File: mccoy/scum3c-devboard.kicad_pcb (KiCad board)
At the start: 2 copper layers, 42.5 x 34.3 mm, 51 parts, among them J1 Conn_02x08_Odd_Even, J10 through_hole, J11 through_hole, J12 through_hole, J13 through_hole, J14 through_hole, J15 through_hole, J16 through_hole, J17 through_hole, J18 through_hole, J19 through_hole, J2 Conn_02x10_Odd_Even, J20 through_hole, J21 through_hole, J3 Conn_02x05_Odd_Even, J4 Conn_01x01_Male, J5 through_hole, J6 through_hole, J7 through_hole, J8 through_hole, J9 through_hole, U1 scum3, U2 TPS60500DGS, U9AB1 ICM-20948

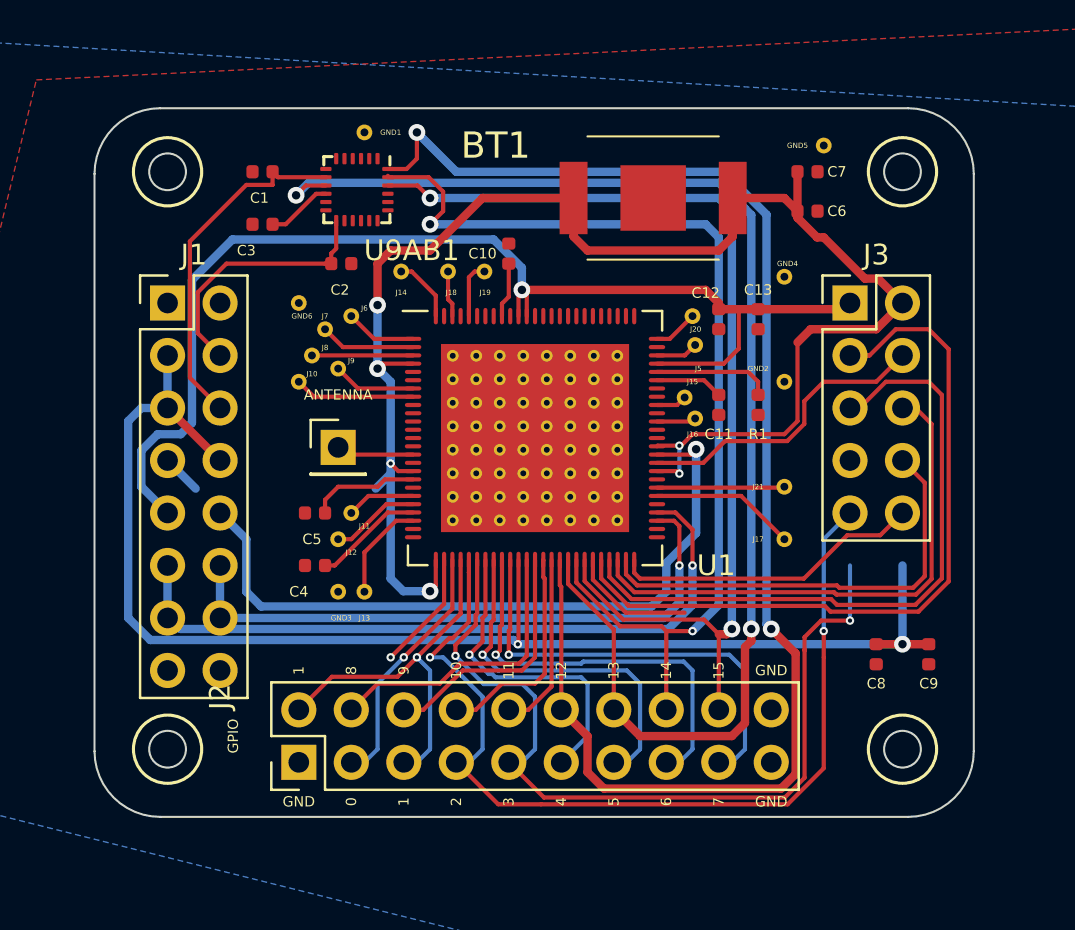
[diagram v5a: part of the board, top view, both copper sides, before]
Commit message: cleared all tracks
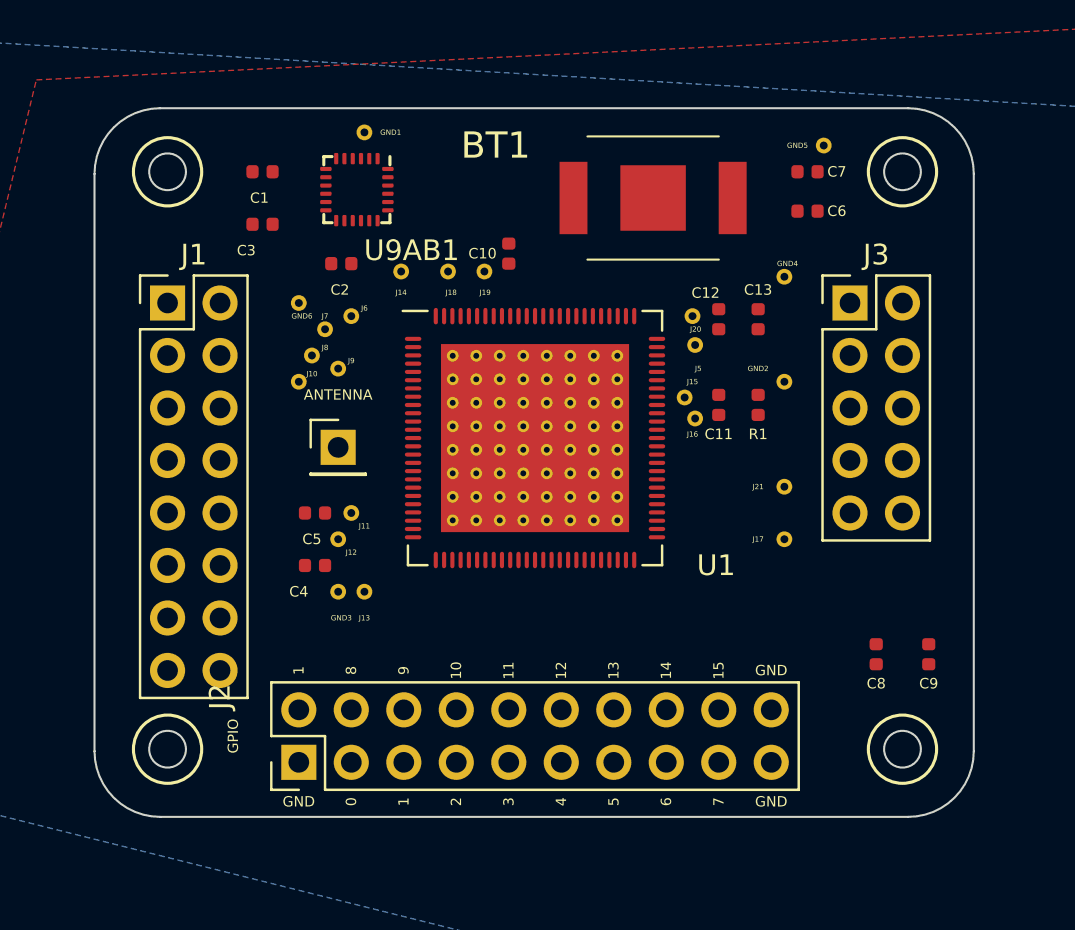
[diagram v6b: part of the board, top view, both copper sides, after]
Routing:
- net +VBAT: track 80.0 -> 0.00 mm, vias 6 -> 0
- net /GPIO12: track 70.6 -> 0.00 mm, vias 2 -> 0
- net +VDDIO: track 66.3 -> 0.00 mm, vias 2 -> 0
- net /GPIO13: track 64.6 -> 0.00 mm, vias 2 -> 0
- net +VDDD: track 57.3 -> 0.00 mm, vias 1 -> 0
- net /GPIO15: track 50.4 -> 0.00 mm, vias 2 -> 0
- net /GPIO14: track 50.2 -> 0.00 mm, vias 2 -> 0
- net /GPIO2: track 45.2 -> 0.00 mm, vias 2 -> 0
- net /GPIO3: track 41.3 -> 0.00 mm, vias 2 -> 0
- net /RsTx: track 36.0 -> 0.00 mm
- net /BOOT_SOURCE_SEL: track 35.0 -> 0.00 mm, vias 1 -> 0
- net /SENSOR_EXT_IN: track 34.3 -> 0.00 mm, vias 1 -> 0
- net /RsRx: track 32.1 -> 0.00 mm
- net /SENSOR_LDO_OUTPUT: track 29.6 -> 0.00 mm, vias 1 -> 0
- net /3WB_CLK: track 25.9 -> 0.00 mm
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
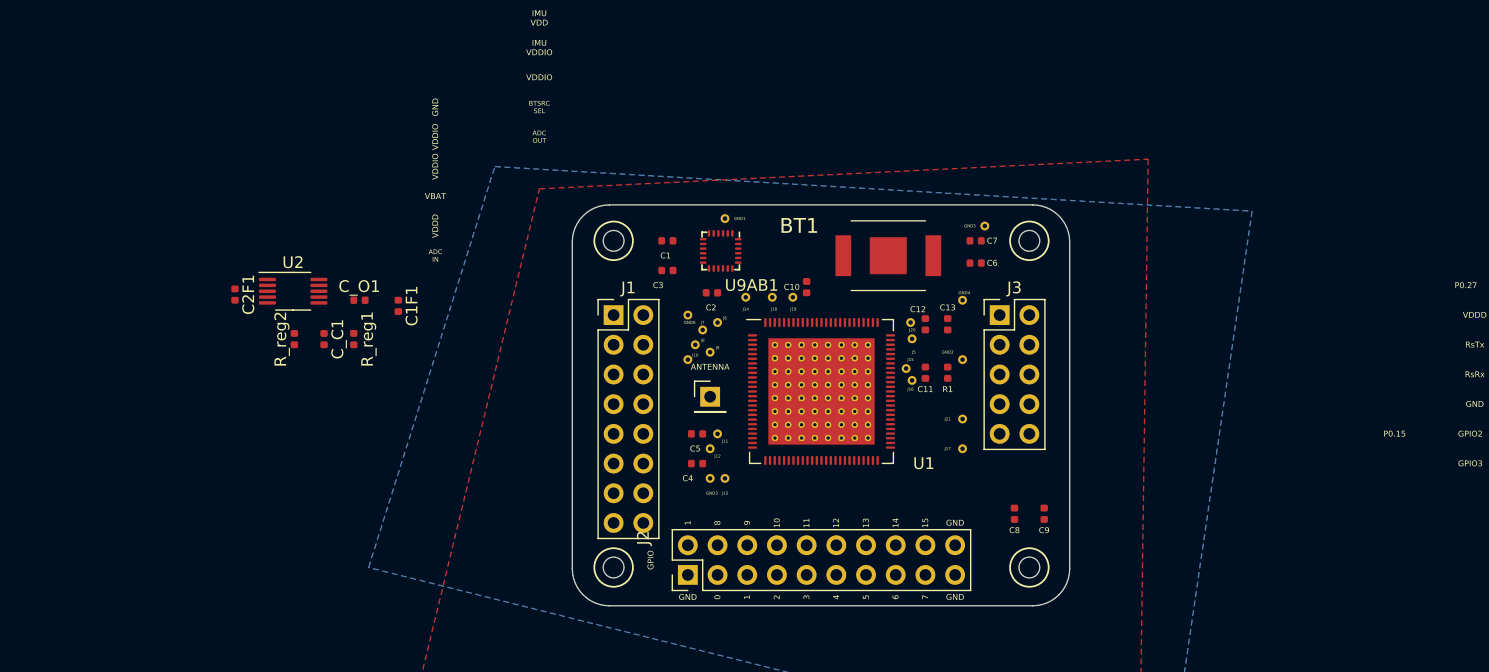
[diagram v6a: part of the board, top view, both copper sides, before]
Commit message: moved some footprints
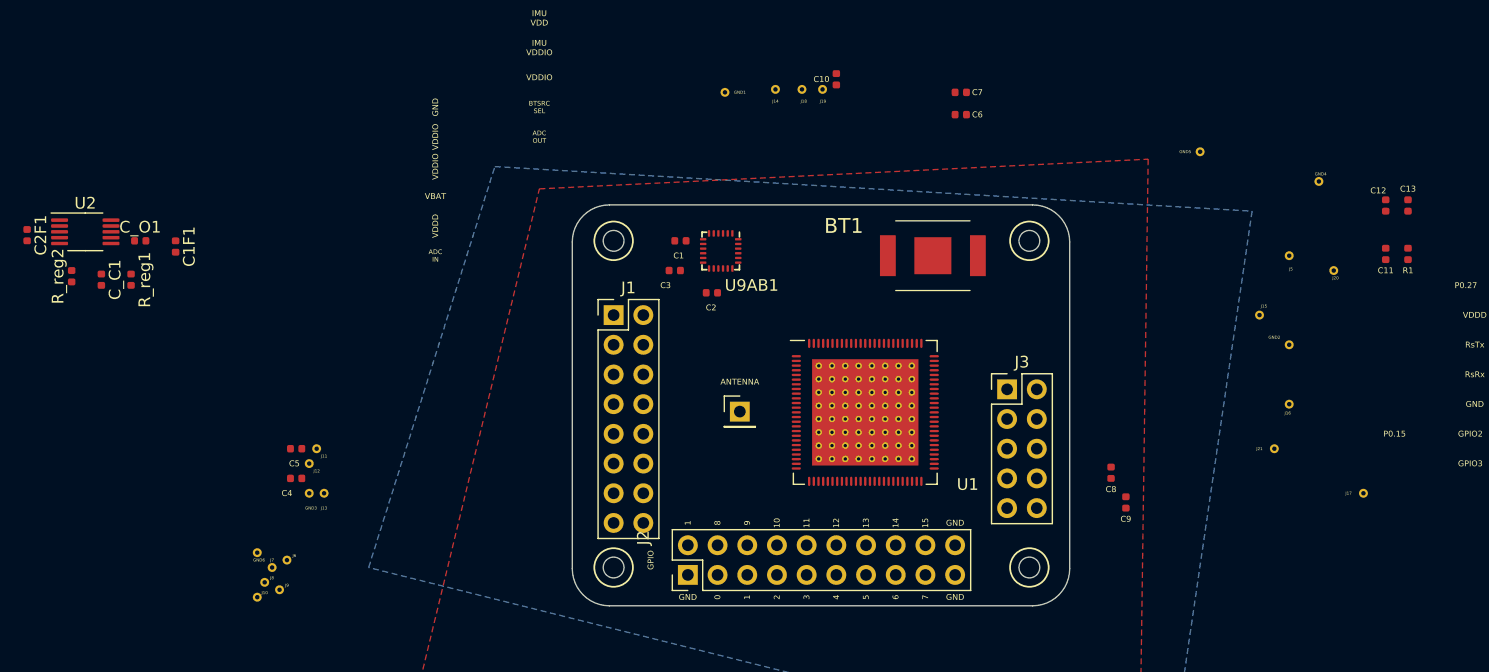
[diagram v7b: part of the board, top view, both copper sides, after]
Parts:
- moved GND6 42.1 mm to (78.1, 104.1)
- moved J10 42.1 mm to (78.1, 108.0)
- moved J6 42.1 mm to (80.6, 104.8)
- moved J8 42.1 mm to (78.7, 106.7)
- moved J7 42.1 mm to (79.4, 105.4)
- moved J9 42.1 mm to (80.0, 107.3)
- moved C11 40.7 mm to (174.6, 78.6)
- moved C12 40.7 mm to (174.6, 74.4)
- moved C13 40.7 mm to (176.5, 74.4)
- moved R1 40.7 mm to (176.5, 78.6)
- moved J20 36.5 mm to (170.2, 80.0)
- moved J17 34.5 mm to (172.7, 99.1)
- moved GND3 34.3 mm to (82.5, 99.1)
- moved J12 34.3 mm to (82.5, 96.5)
- moved J13 34.3 mm to (83.8, 99.1)
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
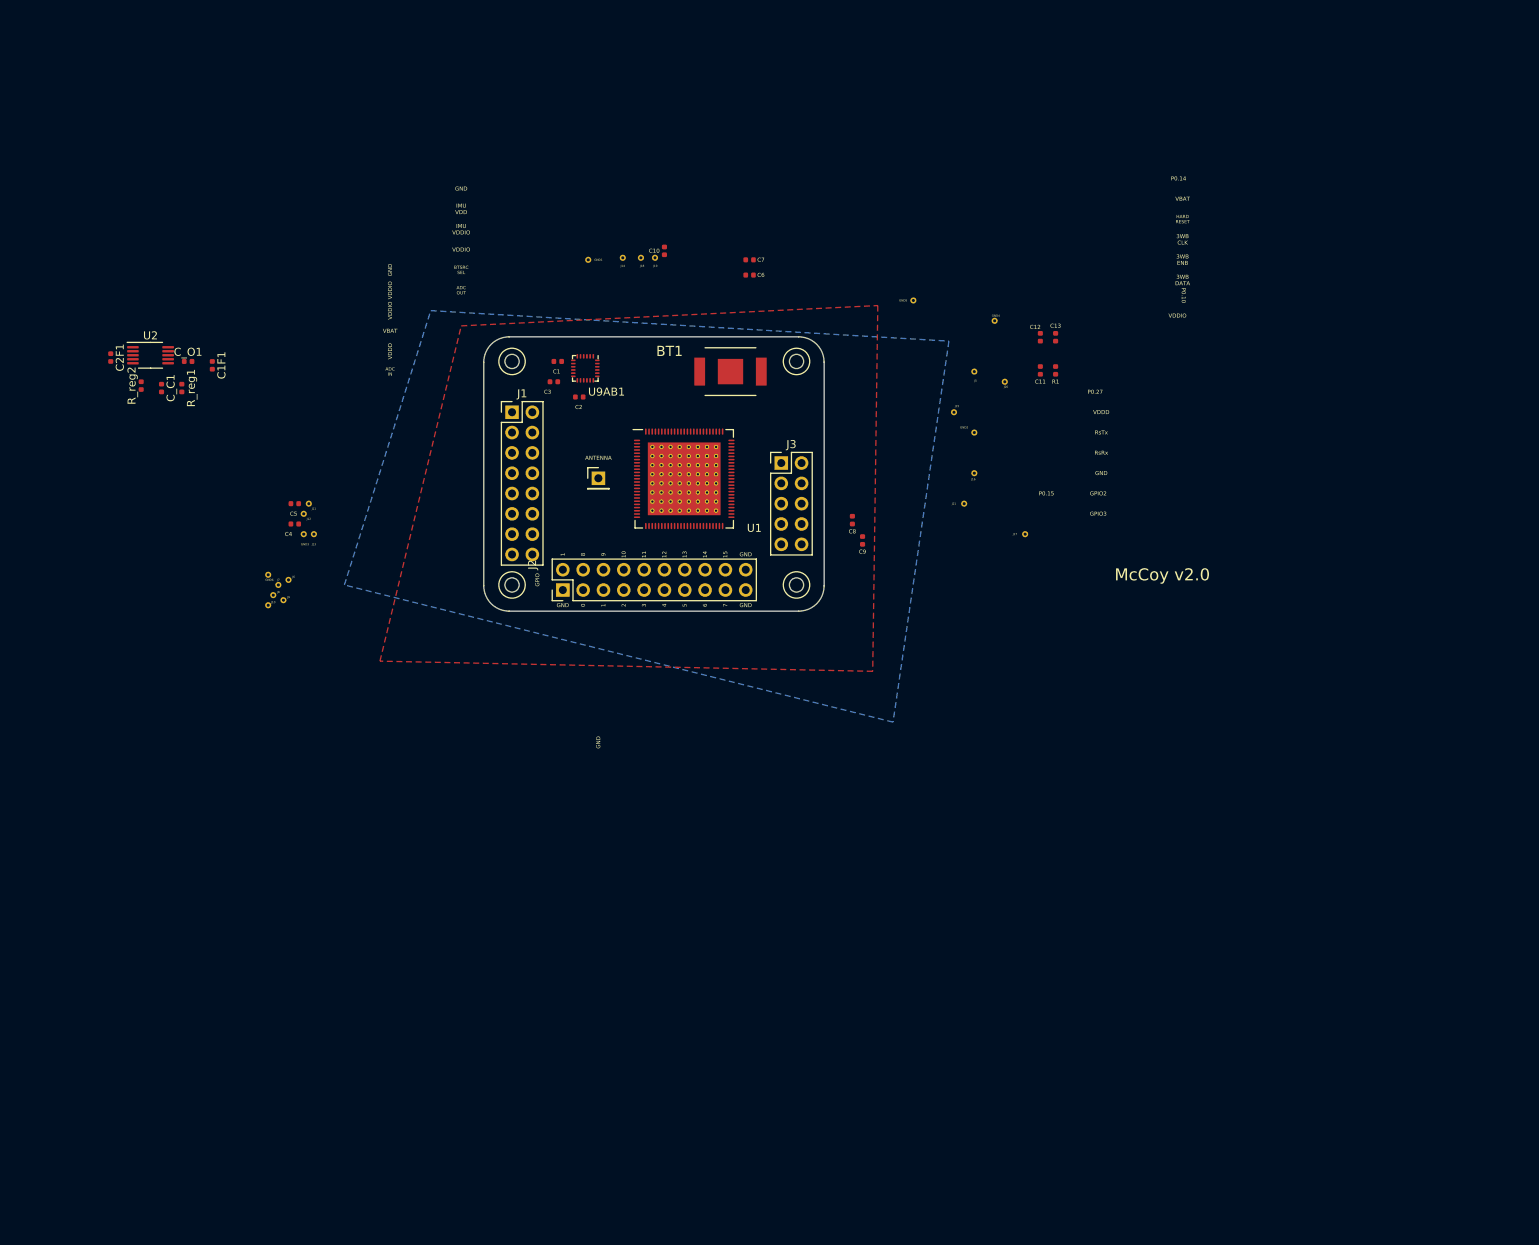
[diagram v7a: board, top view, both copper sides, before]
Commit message: added voltage divider to nrf_vddd
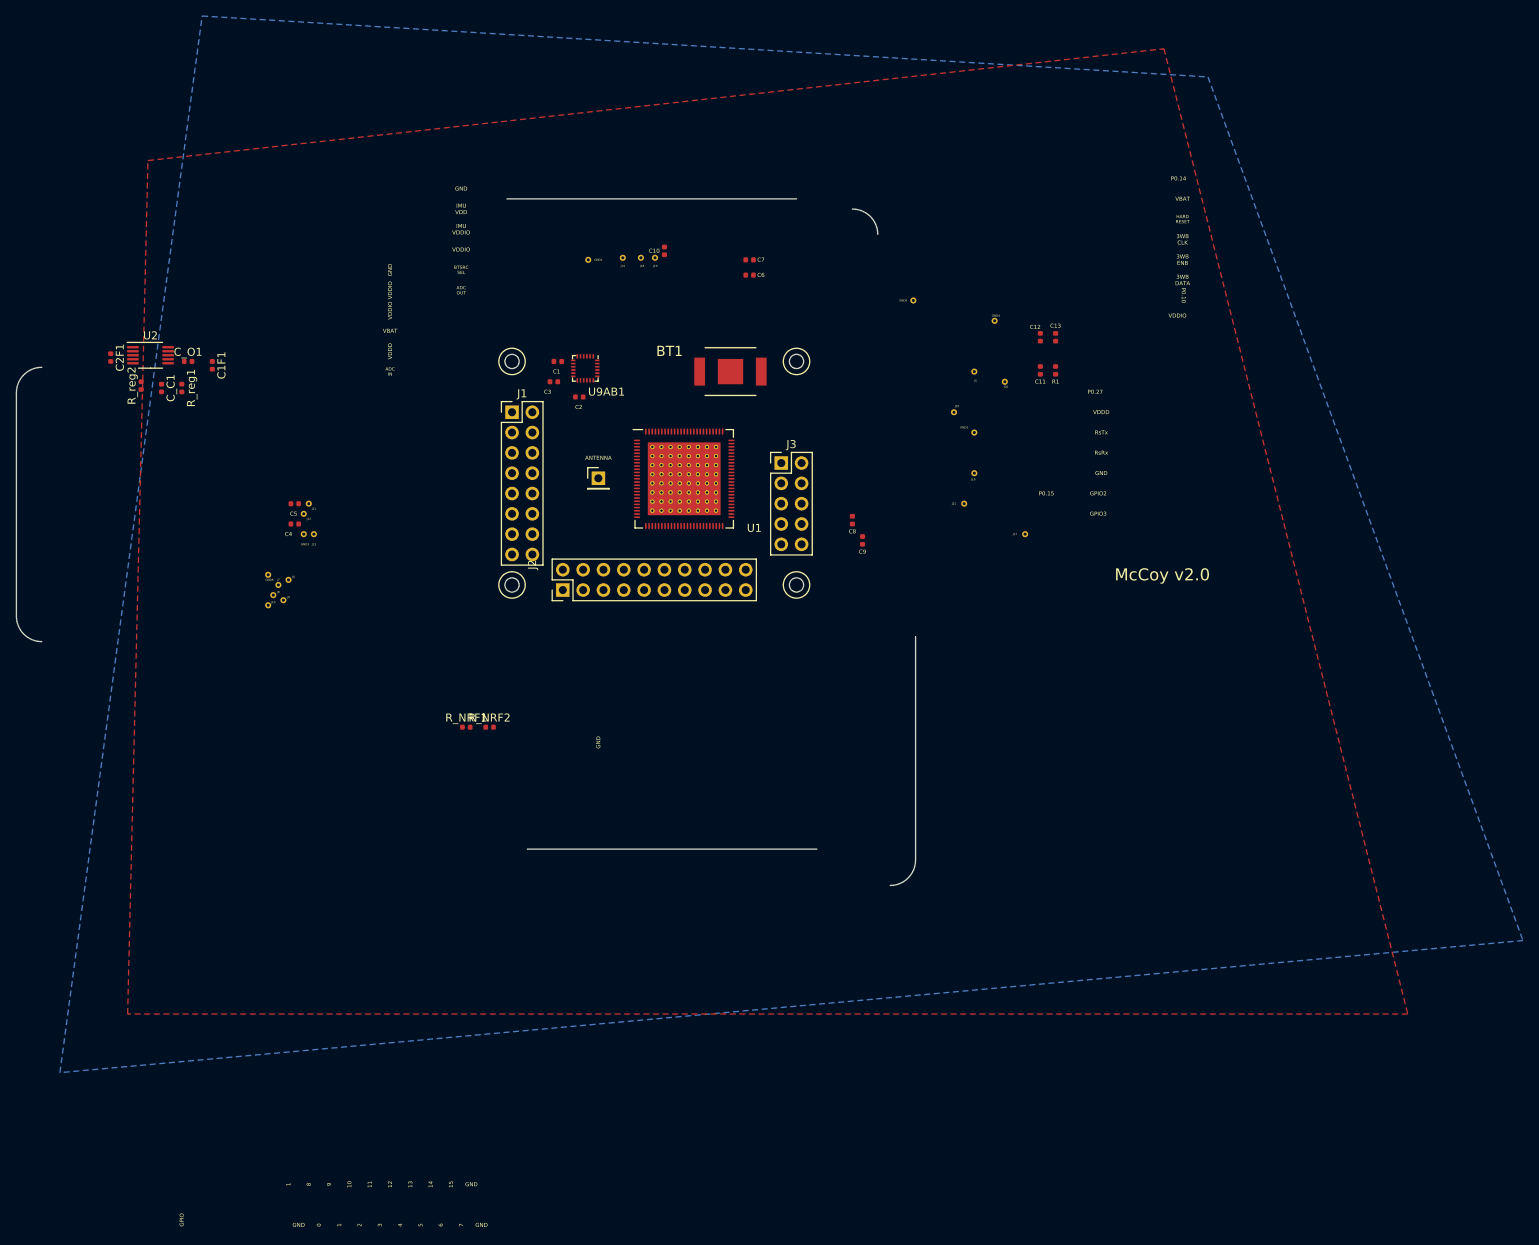
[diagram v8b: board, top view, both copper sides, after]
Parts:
- added R_NRF1: ?, Resistor_SMD:R_0402_1005Metric, F.Cu at (102.9, 123.2)
- added R_NRF2: ?, Resistor_SMD:R_0402_1005Metric, F.Cu at (105.8, 123.2)
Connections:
- J3 pad 1: +VDDD -> Net-(J3-Pad1)
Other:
- board size 42.5 x 34.3 mm -> 112.4 x 85.8 mm
